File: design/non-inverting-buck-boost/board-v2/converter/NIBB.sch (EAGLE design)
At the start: 10 parts

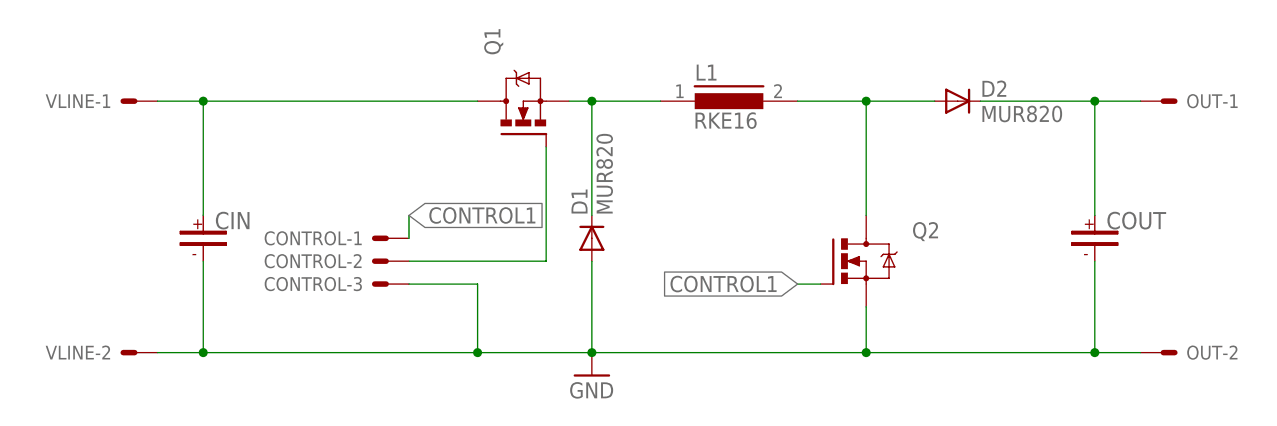
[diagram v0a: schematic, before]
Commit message: updated mosfet conections
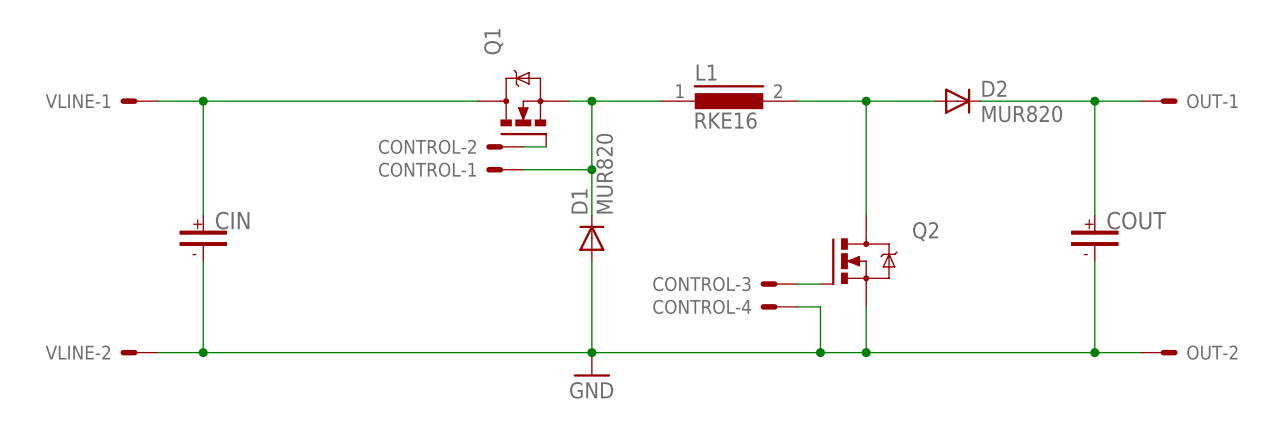
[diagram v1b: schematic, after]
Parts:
- CONTROL: value 22-23-2031 -> 22-23-2041; device con-molex:22-23-2031 -> con-molex:22-23-2041
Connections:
- net CONTROL2 renamed N$4
- removed net CONTROL1: CONTROL-1.S, Q2.G
- new net N$5: CONTROL-3.S, Q2.G
- net GND: now also CONTROL-4.S; no longer CONTROL-3.S
- net N$1: now also CONTROL-1.S
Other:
- moved on the sheet: CONTROL-1, CONTROL-2, CONTROL-3
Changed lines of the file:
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@@
 <setting verticaltext="up"/>
 </settings>
-<grid distance="0.1" unitdist="inch" unit="inch" style="lines" multiple="1" display="yes" altdistance="0.01" altunitdist="inch" altunit="inch"/>
+<grid distance="0.1" unitdist="inch" unit="inch" style="lines" multiple="1" display="no" altdistance="0.01" altunitdist="inch" altunit="inch"/>
 <layers>
 <layer number="1" name="Top" color="4" fill="1" visible="no" active="no"/>
@@
 <part name="Q2" library="felippe" deviceset="IRF640" device=""/>
 <part name="GND1" library="supply1" deviceset="GND" device=""/>
-<part name="CONTROL" library="con-molex" deviceset="22-23-2031" device=""/>
 <part name="CIN" library="capacitor" deviceset="CAPP-U" device="F"/>
+<part name="CONTROL" library="con-molex" deviceset="22-23-2041" device=""/>
 </parts>
 <sheets>
@@
 <instance part="Q2" gate="G$1" x="53.34" y="45.72"/>
 <instance part="GND1" gate="1" x="25.4" y="33.02"/>
-<instance part="CONTROL" gate="-1" x="2.54" y="48.26" smashed="yes" rot="R180">
-<attribute name="NAME" x="0" y="49.022" size="1.524" layer="95" rot="R180"/>
+<instance part="CIN" gate="G$1" x="-17.78" y="48.26"/>
+<instance part="CONTROL" gate="-1" x="15.24" y="55.88" smashed="yes" rot="R180">
+<attribute name="NAME" x="12.7" y="56.642" size="1.524" layer="95" rot="R180"/>
 </instance>
-<instance part="CONTROL" gate="-2" x="2.54" y="45.72" rot="R180"/>
-<instance part="CONTROL" gate="-3" x="2.54" y="43.18" rot="R180"/>
-<instance part="CIN" gate="G$1" x="-17.78" y="48.26"/>
+<instance part="CONTROL" gate="-2" x="15.24" y="58.42" rot="R180"/>
+<instance part="CONTROL" gate="-3" x="45.72" y="43.18" rot="R180"/>
+<instance part="CONTROL" gate="-4" x="45.72" y="40.64" rot="R180"/>
 </instances>
 <busses>
@@
 </segment>
 </net>
-<net name="CONTROL1" class="0">
-<segment>
-<pinref part="Q2" gate="G$1" pin="G"/>
-<wire x1="50.8" y1="43.18" x2="48.26" y2="43.18" width="0.1524" layer="91"/>
-<label x="48.26" y="43.18" size="1.778" layer="95" rot="R180" xref="yes"/>
-</segment>
-<segment>
-<pinref part="CONTROL" gate="-1" pin="S"/>
-<wire x1="5.08" y1="48.26" x2="5.08" y2="50.8" width="0.1524" layer="91"/>
-<label x="5.08" y="50.8" size="1.778" layer="95" xref="yes"/>
-</segment>
-</net>
 <net name="N$7" class="0">
 <segment>
@@
 <pinref part="D1" gate="1" pin="C"/>
 <wire x1="25.4" y1="63.5" x2="33.02" y2="63.5" width="0.1524" layer="91"/>
-<wire x1="25.4" y1="50.8" x2="25.4" y2="63.5" width="0.1524" layer="91"/>
 <junction x="25.4" y="63.5"/>
 <pinref part="Q1" gate="G$1" pin="S"/>
+<wire x1="25.4" y1="50.8" x2="25.4" y2="55.88" width="0.1524" layer="91"/>
+<pinref part="CONTROL" gate="-1" pin="S"/>
+<wire x1="25.4" y1="55.88" x2="25.4" y2="63.5" width="0.1524" layer="91"/>
+<wire x1="17.78" y1="55.88" x2="25.4" y2="55.88" width="0.1524" layer="91"/>
+<junction x="25.4" y="55.88"/>
 </segment>
 </net>
@@
 <wire x1="-22.86" y1="35.56" x2="-17.78" y2="35.56" width="0.1524" layer="91"/>
 <pinref part="COUT" gate="G$1" pin="-"/>
-<wire x1="-17.78" y1="35.56" x2="12.7" y2="35.56" width="0.1524" layer="91"/>
-<wire x1="12.7" y1="35.56" x2="25.4" y2="35.56" width="0.1524" layer="91"/>
-<wire x1="25.4" y1="35.56" x2="55.88" y2="35.56" width="0.1524" layer="91"/>
+<wire x1="-17.78" y1="35.56" x2="25.4" y2="35.56" width="0.1524" layer="91"/>
+<wire x1="25.4" y1="35.56" x2="50.8" y2="35.56" width="0.1524" layer="91"/>
+<wire x1="50.8" y1="35.56" x2="55.88" y2="35.56" width="0.1524" layer="91"/>
 <wire x1="81.28" y1="45.72" x2="81.28" y2="35.56" width="0.1524" layer="91"/>
 <wire x1="81.28" y1="35.56" x2="55.88" y2="35.56" width="0.1524" layer="91"/>
@@
 <pinref part="Q2" gate="G$1" pin="S"/>
 <pinref part="GND1" gate="1" pin="GND"/>
-<pinref part="CONTROL" gate="-3" pin="S"/>
-<wire x1="5.08" y1="43.18" x2="12.7" y2="43.18" width="0.1524" layer="91"/>
-<wire x1="12.7" y1="43.18" x2="12.7" y2="35.56" width="0.1524" layer="91"/>
-<junction x="12.7" y="35.56"/>
 <pinref part="CIN" gate="G$1" pin="-"/>
 <wire x1="-17.78" y1="45.72" x2="-17.78" y2="35.56" width="0.1524" layer="91"/>
 <junction x="-17.78" y="35.56"/>
-</segment>
-</net>
-<net name="CONTROL2" class="0">
+<wire x1="50.8" y1="40.64" x2="50.8" y2="35.56" width="0.1524" layer="91"/>
+<junction x="50.8" y="35.56"/>
+<pinref part="CONTROL" gate="-4" pin="S"/>
+<wire x1="48.26" y1="40.64" x2="50.8" y2="40.64" width="0.1524" layer="91"/>
+</segment>
+</net>
+<net name="N$4" class="0">
 <segment>
 <pinref part="CONTROL" gate="-2" pin="S"/>
-<wire x1="5.08" y1="45.72" x2="20.32" y2="45.72" width="0.1524" layer="91"/>
 <pinref part="Q1" gate="G$1" pin="G"/>
-<wire x1="20.32" y1="45.72" x2="20.32" y2="58.42" width="0.1524" layer="91"/>
-</segment>
-</net>
+<wire x1="17.78" y1="58.42" x2="20.32" y2="58.42" width="0.1524" layer="91"/>
+</segment>
+</net>
+<net name="N$5" class="0">
+<segment>
+<pinref part="CONTROL" gate="-3" pin="S"/>
+<pinref part="Q2" gate="G$1" pin="G"/>
+<wire x1="48.26" y1="43.18" x2="50.8" y2="43.18" width="0.1524" layer="91"/>
+</segment>
+</net>

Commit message: revert commit
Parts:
- CONTROL: value 22-23-2041 -> 22-23-2031; device con-molex:22-23-2041 -> con-molex:22-23-2031
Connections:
- net N$4 renamed CONTROL2
- removed net N$5: CONTROL-3.S, Q2.G
- new net CONTROL1: CONTROL-1.S, Q2.G
- net GND: now also CONTROL-3.S; no longer CONTROL-4.S
- net N$1: no longer CONTROL-1.S
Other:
- moved on the sheet: CONTROL-1, CONTROL-2, CONTROL-3
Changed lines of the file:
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@@
 <setting verticaltext="up"/>
 </settings>
-<grid distance="0.1" unitdist="inch" unit="inch" style="lines" multiple="1" display="no" altdistance="0.01" altunitdist="inch" altunit="inch"/>
+<grid distance="0.1" unitdist="inch" unit="inch" style="lines" multiple="1" display="yes" altdistance="0.01" altunitdist="inch" altunit="inch"/>
 <layers>
 <layer number="1" name="Top" color="4" fill="1" visible="no" active="no"/>
@@
 <part name="Q2" library="felippe" deviceset="IRF640" device=""/>
 <part name="GND1" library="supply1" deviceset="GND" device=""/>
+<part name="CONTROL" library="con-molex" deviceset="22-23-2031" device=""/>
 <part name="CIN" library="capacitor" deviceset="CAPP-U" device="F"/>
-<part name="CONTROL" library="con-molex" deviceset="22-23-2041" device=""/>
 </parts>
 <sheets>
@@
 <instance part="Q2" gate="G$1" x="53.34" y="45.72"/>
 <instance part="GND1" gate="1" x="25.4" y="33.02"/>
+<instance part="CONTROL" gate="-1" x="2.54" y="48.26" smashed="yes" rot="R180">
+<attribute name="NAME" x="0" y="49.022" size="1.524" layer="95" rot="R180"/>
+</instance>
+<instance part="CONTROL" gate="-2" x="2.54" y="45.72" rot="R180"/>
+<instance part="CONTROL" gate="-3" x="2.54" y="43.18" rot="R180"/>
 <instance part="CIN" gate="G$1" x="-17.78" y="48.26"/>
-<instance part="CONTROL" gate="-1" x="15.24" y="55.88" smashed="yes" rot="R180">
-<attribute name="NAME" x="12.7" y="56.642" size="1.524" layer="95" rot="R180"/>
-</instance>
-<instance part="CONTROL" gate="-2" x="15.24" y="58.42" rot="R180"/>
-<instance part="CONTROL" gate="-3" x="45.72" y="43.18" rot="R180"/>
-<instance part="CONTROL" gate="-4" x="45.72" y="40.64" rot="R180"/>
 </instances>
 <busses>
@@
 </segment>
 </net>
+<net name="CONTROL1" class="0">
+<segment>
+<pinref part="Q2" gate="G$1" pin="G"/>
+<wire x1="50.8" y1="43.18" x2="48.26" y2="43.18" width="0.1524" layer="91"/>
+<label x="48.26" y="43.18" size="1.778" layer="95" rot="R180" xref="yes"/>
+</segment>
+<segment>
+<pinref part="CONTROL" gate="-1" pin="S"/>
+<wire x1="5.08" y1="48.26" x2="5.08" y2="50.8" width="0.1524" layer="91"/>
+<label x="5.08" y="50.8" size="1.778" layer="95" xref="yes"/>
+</segment>
+</net>
 <net name="N$7" class="0">
 <segment>
@@
 <pinref part="D1" gate="1" pin="C"/>
 <wire x1="25.4" y1="63.5" x2="33.02" y2="63.5" width="0.1524" layer="91"/>
+<wire x1="25.4" y1="50.8" x2="25.4" y2="63.5" width="0.1524" layer="91"/>
 <junction x="25.4" y="63.5"/>
 <pinref part="Q1" gate="G$1" pin="S"/>
-<wire x1="25.4" y1="50.8" x2="25.4" y2="55.88" width="0.1524" layer="91"/>
-<pinref part="CONTROL" gate="-1" pin="S"/>
-<wire x1="25.4" y1="55.88" x2="25.4" y2="63.5" width="0.1524" layer="91"/>
-<wire x1="17.78" y1="55.88" x2="25.4" y2="55.88" width="0.1524" layer="91"/>
-<junction x="25.4" y="55.88"/>
 </segment>
 </net>
@@
 <wire x1="-22.86" y1="35.56" x2="-17.78" y2="35.56" width="0.1524" layer="91"/>
 <pinref part="COUT" gate="G$1" pin="-"/>
-<wire x1="-17.78" y1="35.56" x2="25.4" y2="35.56" width="0.1524" layer="91"/>
-<wire x1="25.4" y1="35.56" x2="50.8" y2="35.56" width="0.1524" layer="91"/>
-<wire x1="50.8" y1="35.56" x2="55.88" y2="35.56" width="0.1524" layer="91"/>
+<wire x1="-17.78" y1="35.56" x2="12.7" y2="35.56" width="0.1524" layer="91"/>
+<wire x1="12.7" y1="35.56" x2="25.4" y2="35.56" width="0.1524" layer="91"/>
+<wire x1="25.4" y1="35.56" x2="55.88" y2="35.56" width="0.1524" layer="91"/>
 <wire x1="81.28" y1="45.72" x2="81.28" y2="35.56" width="0.1524" layer="91"/>
 <wire x1="81.28" y1="35.56" x2="55.88" y2="35.56" width="0.1524" layer="91"/>
@@
 <pinref part="Q2" gate="G$1" pin="S"/>
 <pinref part="GND1" gate="1" pin="GND"/>
+<pinref part="CONTROL" gate="-3" pin="S"/>
+<wire x1="5.08" y1="43.18" x2="12.7" y2="43.18" width="0.1524" layer="91"/>
+<wire x1="12.7" y1="43.18" x2="12.7" y2="35.56" width="0.1524" layer="91"/>
+<junction x="12.7" y="35.56"/>
 <pinref part="CIN" gate="G$1" pin="-"/>
 <wire x1="-17.78" y1="45.72" x2="-17.78" y2="35.56" width="0.1524" layer="91"/>
 <junction x="-17.78" y="35.56"/>
-<wire x1="50.8" y1="40.64" x2="50.8" y2="35.56" width="0.1524" layer="91"/>
-<junction x="50.8" y="35.56"/>
-<pinref part="CONTROL" gate="-4" pin="S"/>
-<wire x1="48.26" y1="40.64" x2="50.8" y2="40.64" width="0.1524" layer="91"/>
-</segment>
-</net>
-<net name="N$4" class="0">
+</segment>
+</net>
+<net name="CONTROL2" class="0">
 <segment>
 <pinref part="CONTROL" gate="-2" pin="S"/>
+<wire x1="5.08" y1="45.72" x2="20.32" y2="45.72" width="0.1524" layer="91"/>
 <pinref part="Q1" gate="G$1" pin="G"/>
-<wire x1="17.78" y1="58.42" x2="20.32" y2="58.42" width="0.1524" layer="91"/>
-</segment>
-</net>
-<net name="N$5" class="0">
-<segment>
-<pinref part="CONTROL" gate="-3" pin="S"/>
-<pinref part="Q2" gate="G$1" pin="G"/>
-<wire x1="48.26" y1="43.18" x2="50.8" y2="43.18" width="0.1524" layer="91"/>
-</segment>
-</net>
+<wire x1="20.32" y1="45.72" x2="20.32" y2="58.42" width="0.1524" layer="91"/>
+</segment>
+</net>
